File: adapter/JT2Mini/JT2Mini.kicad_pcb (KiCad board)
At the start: 2 copper layers, 35 x 24 mm, 5 parts, among them J1 CBE224, J2 3220-10-0300-00

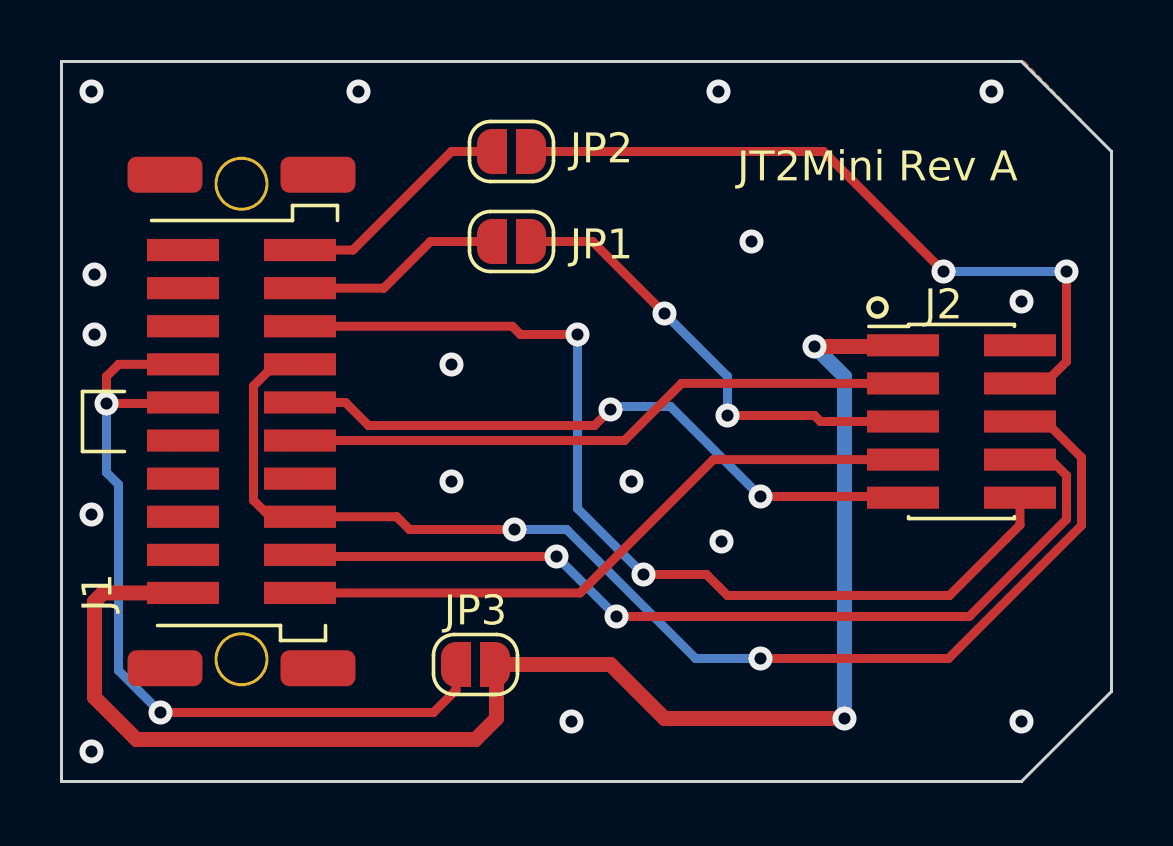
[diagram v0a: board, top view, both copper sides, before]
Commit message: Rev B PCB - added test points and GND for checking signal integrity
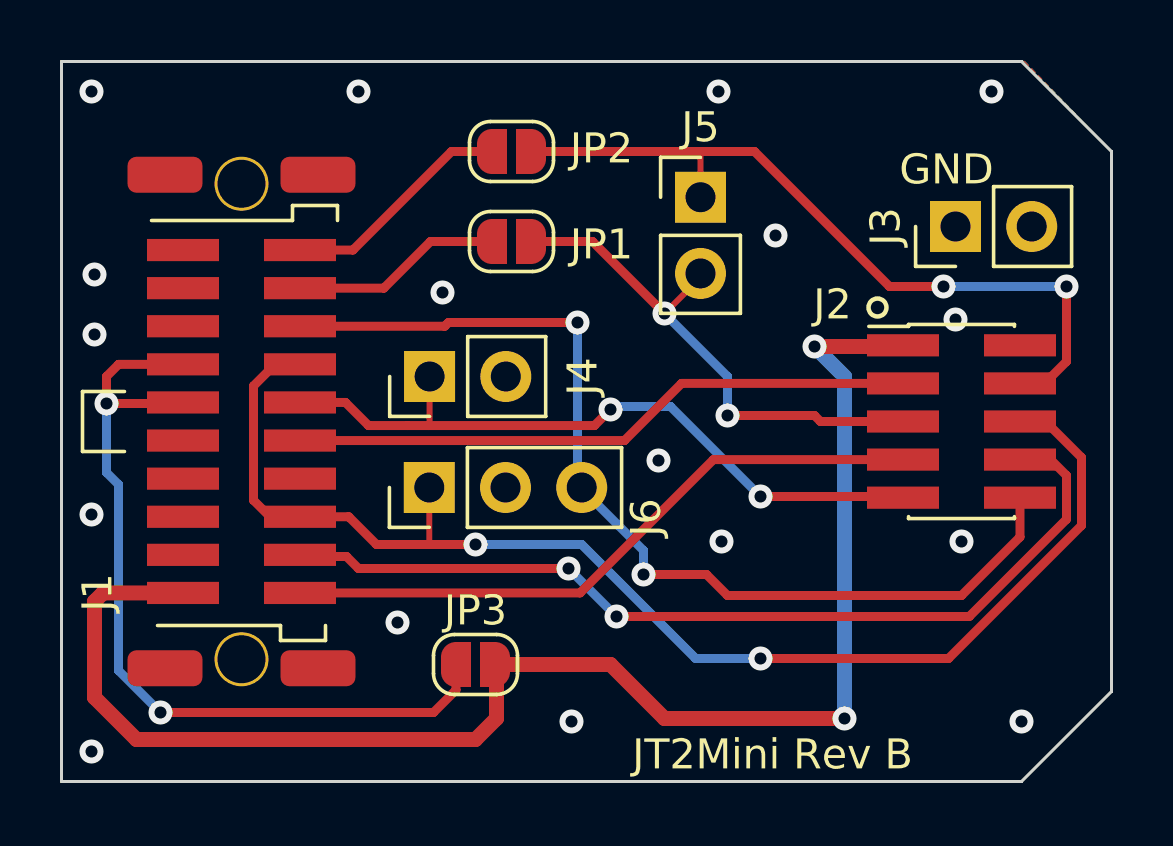
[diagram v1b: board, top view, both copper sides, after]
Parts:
- added J3: Conn_01x02, Connector_PinHeader_2.54mm:PinHeader_1x02_P2.54mm_Vertical, F.Cu at (148.8, 103.5)
- added J4: Conn_01x02, Connector_PinHeader_2.54mm:PinHeader_1x02_P2.54mm_Vertical, F.Cu at (131.3, 108.5)
- added J5: Conn_01x02, Connector_PinHeader_2.54mm:PinHeader_1x02_P2.54mm_Vertical, F.Cu at (140.3, 102.5)
- added J6: Conn_01x03, Connector_PinHeader_2.54mm:PinHeader_1x03_P2.54mm_Vertical, F.Cu at (131.3, 112.2)
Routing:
- net /SWO_TRACED1: track 42.1 -> 44.0 mm
- net /TX: track 15.6 -> 17.5 mm
- net /TRACECLK: track 21.9 -> 23.6 mm
- net /RX: track 24.4 -> 25.6 mm
- net GND: vias 16 -> 17
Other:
- board text added: "D1"
- board text added: "D2"
- board text added: "GND"
- board text added: "JT2Mini Rev B"
- board text added: "RX"
- board text added: "TRACECLK"
- board text added: "TX"
- board text added: "VCOM"
- board text removed: "JT2Mini Rev A"
